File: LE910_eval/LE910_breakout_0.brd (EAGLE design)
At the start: 2 parts, among them M1 LE910_V2_BREAKOUT_CASEDGES, U1 LE910_V2

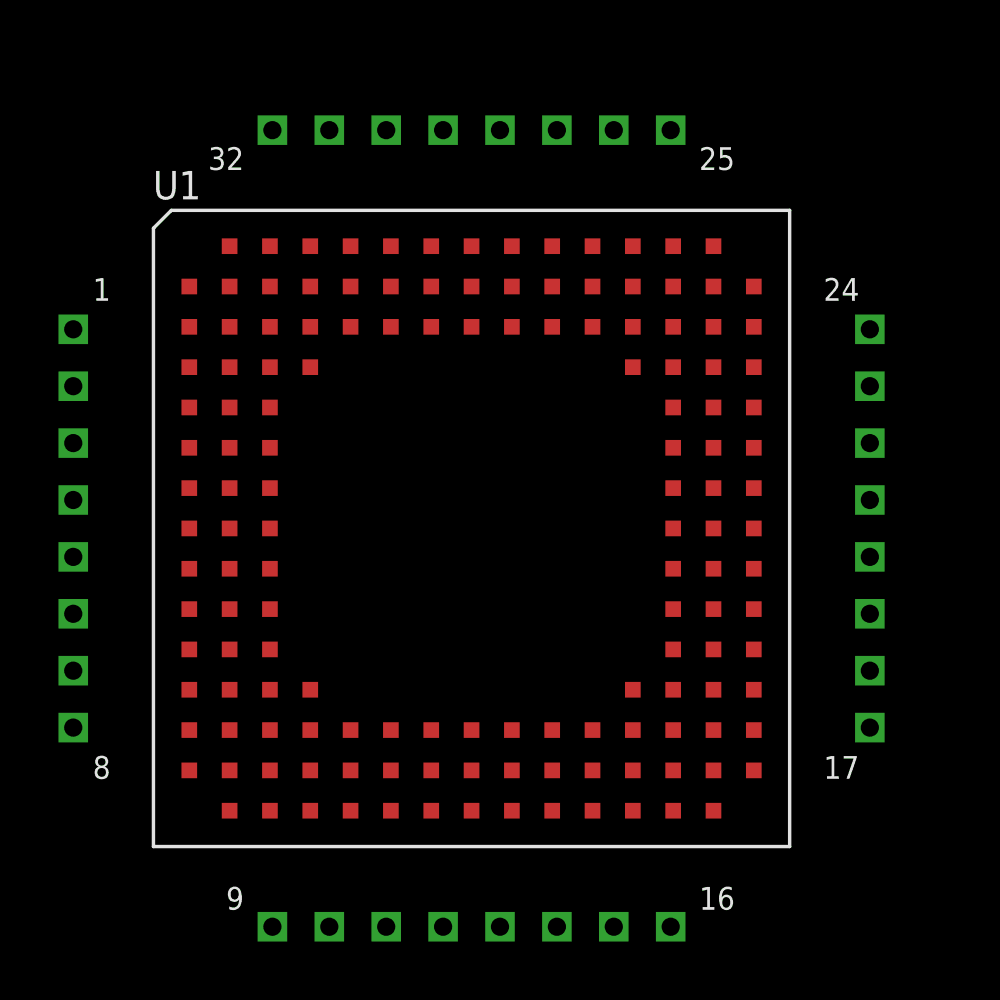
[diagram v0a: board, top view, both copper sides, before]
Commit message: デザイン修正
・ブレークアウト基板のピンレイアウトを修正
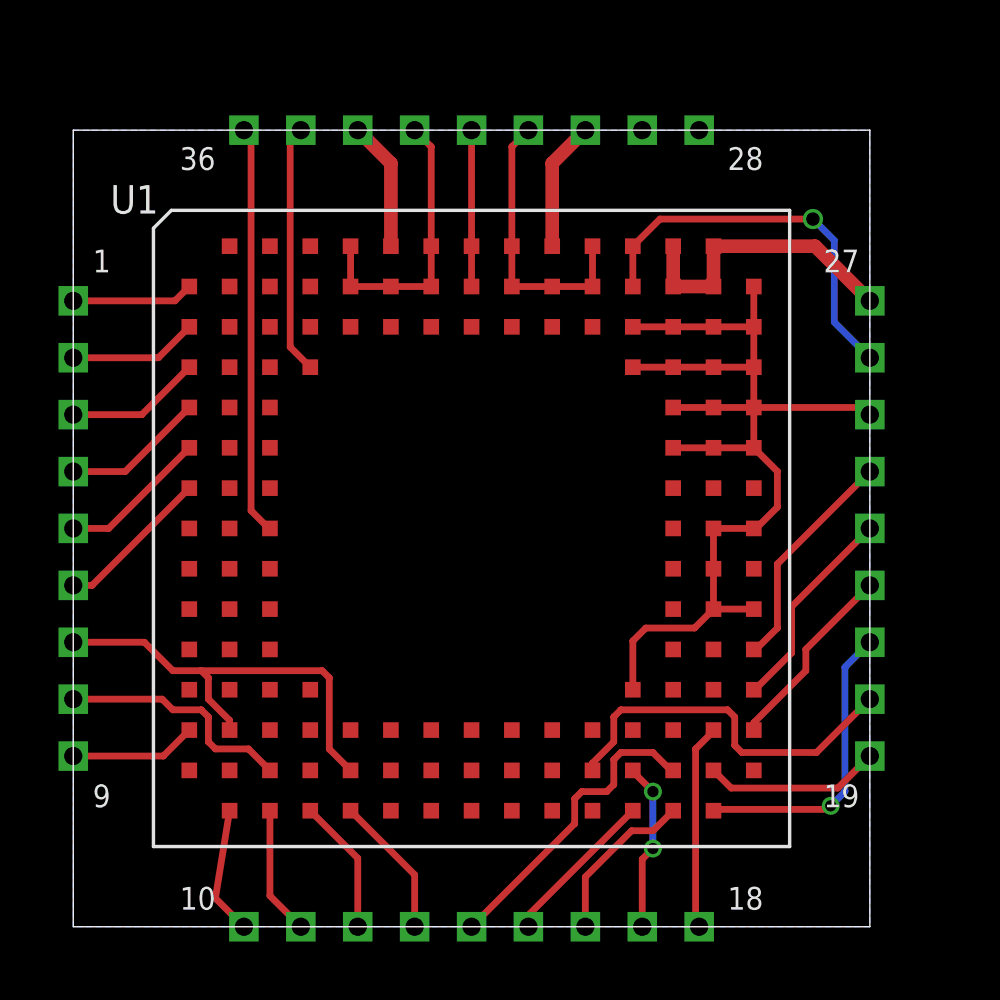
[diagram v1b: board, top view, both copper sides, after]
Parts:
- M1: value LE910_V2_BREAKOUT_CASEDGES -> LE910_V2_BREAKOUT_CASEDG; device Modules:LE910_V2_BREAKOUT_CASEDGES -> Modules:LE910_V2_BREAKOUT_CASEDG
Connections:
- new net USB_D+: M1.10, U1.B15
- new net USB_D-: M1.11, U1.C15
- new net VUSB: M1.9, U1.A13
- net 0V: now also M1.1, M1.18, M1.33, M1.35, M1.7; no longer M1.10, M1.15, M1.22, M1.26
- net ANTENNA: now also M1.30; no longer M1.27
- net ANT_DIV: now also M1.34; no longer M1.30
- net C103/TXD: now also M1.16; no longer M1.13
- net C104/RXD: now also M1.15; no longer M1.12
- net C105/RTS: now also M1.20; no longer M1.17
- net C106/CTS: now also M1.21; no longer M1.18
- net C107/DSR: now also M1.19; no longer M1.16
- net C108/DTR: now also M1.17; no longer M1.14
- net C109/DCD: now also M1.14; no longer M1.11
- net GPIO_01: now also M1.36; no longer M1.1
- net HW_SHUT: now also M1.22; no longer M1.19
- net ON_OFF: now also M1.23; no longer M1.20
- net RX_AUX: now also M1.13; no longer M1.7
- net TX_AUX: now also M1.12; no longer M1.8
- net VAUX: now also M1.24; no longer M1.21
- net VBATT: now also M1.26; no longer M1.23
- net VBATT_PA: now also M1.27; no longer M1.24
- net VRTC: now also M1.8; no longer M1.9
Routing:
- net 0V: track 0.00 -> 126.6 mm
- net GPIO_01: track 0.00 -> 18.3 mm
- net VBATT: track 0.00 -> 17.6 mm, vias 0 -> 1
- net C105/RTS: track 0.00 -> 16.9 mm
- net C109/DCD: track 0.00 -> 13.9 mm
- net VBATT_PA: track 0.00 -> 13.4 mm
- net C106/CTS: track 0.00 -> 13.3 mm, vias 0 -> 1
- net VRTC: track 0.00 -> 10.7 mm
- net VAUX: track 0.00 -> 10.1 mm
- net ON_OFF: track 0.00 -> 9.37 mm
- net HW_SHUT: track 0.00 -> 8.61 mm
- net C107/DSR: track 0.00 -> 7.90 mm
- net C108/DTR: track 0.00 -> 7.58 mm, vias 0 -> 2
- net C103/TXD: track 0.00 -> 7.37 mm
- net C104/RXD: track 0.00 -> 7.11 mm
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- added copper zone on layer 16, net 0V
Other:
- board outline added: 35.6 x 35.6 mm

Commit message: デザイン修正
・配線パターンを見直し
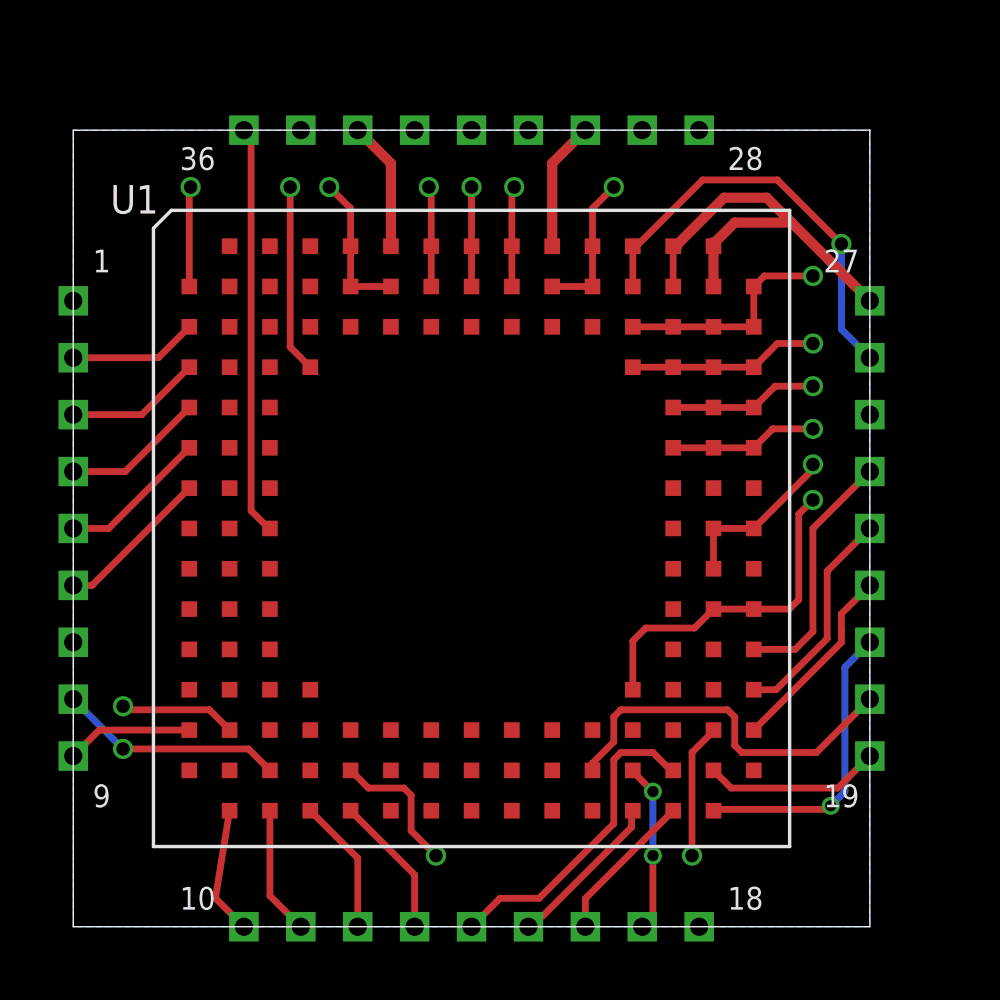
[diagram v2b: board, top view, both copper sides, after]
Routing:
- net 0V: track 126.6 -> 111.6 mm, vias 0 -> 16
- net VBATT_PA: track 13.4 -> 19.2 mm
- net VBATT: track 17.6 -> 19.1 mm
- net VAUX: track 10.1 -> 11.2 mm
- net VRTC: track 10.7 -> 10.1 mm, vias 0 -> 1
- net C103/TXD: track 7.37 -> 6.80 mm
- net ON_OFF: track 9.37 -> 9.93 mm

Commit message: デザイン修正
・パターンを小修正
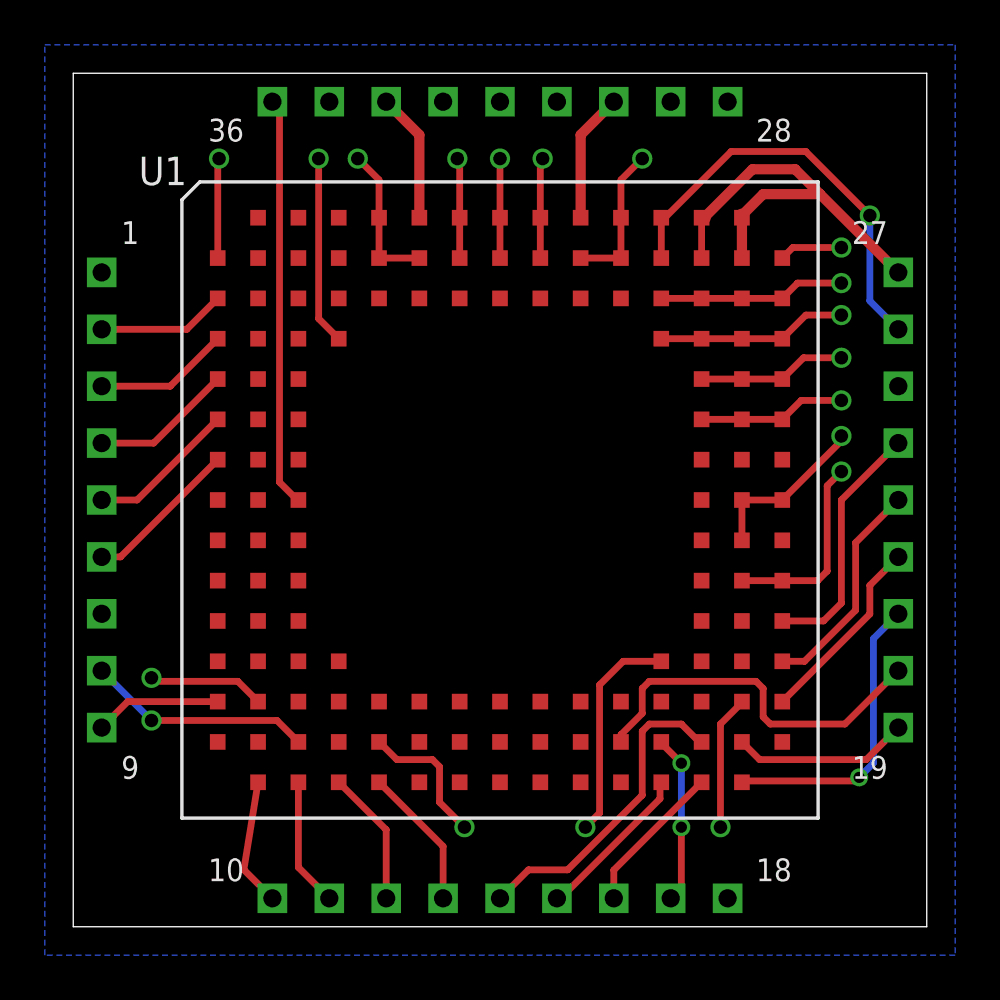
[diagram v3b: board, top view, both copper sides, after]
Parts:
- moved M1 1.80 mm to (1.27, 1.27)
- moved U1 1.80 mm to (19.1, 19.1)
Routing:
- net 0V: track 111.6 -> 116.2 mm, vias 16 -> 18
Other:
- board size 35.6 x 35.6 mm -> 38.1 x 38.1 mm
